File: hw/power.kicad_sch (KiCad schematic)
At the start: 0 parts

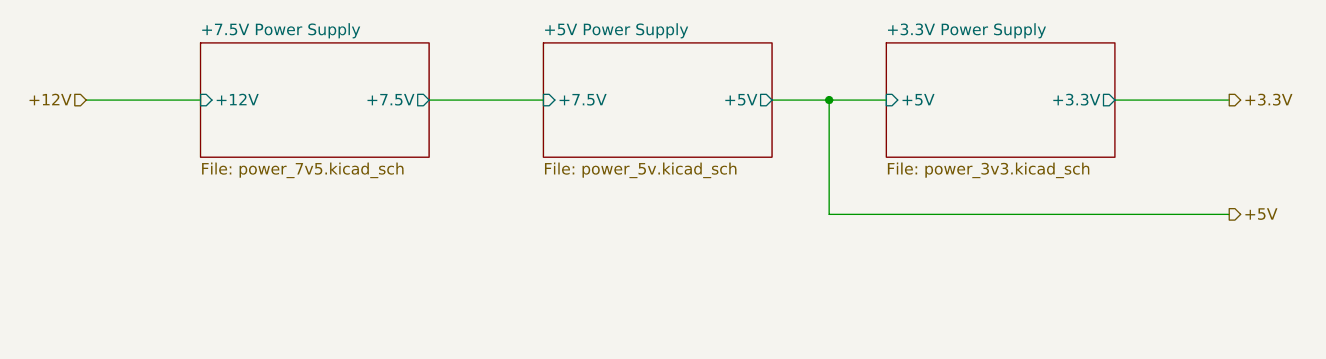
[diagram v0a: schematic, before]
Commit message: hw: top level schematic
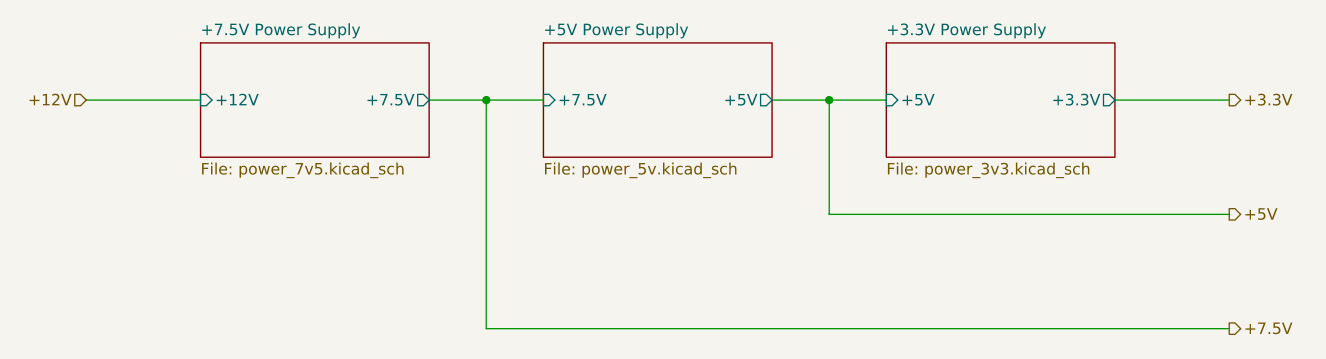
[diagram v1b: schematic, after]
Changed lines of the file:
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@@
+		(color 0 0 0 0)
+	)
+	(junction
+		(at 69.85 57.15)
+		(diameter 0)
 		(color 0 0 0 0)
 	)
 	(wire
 		(pts
-			(xy 63.5 57.15) (xy 76.2 57.15)
+			(xy 63.5 57.15) (xy 69.85 57.15)
 		)
 		(stroke
@@
 		)
 	)
+	(wire
+		(pts
+			(xy 69.85 82.55) (xy 152.4 82.55)
+		)
+		(stroke
+			(width 0)
+			(type default)
+		)
+	)
+	(wire
+		(pts
+			(xy 69.85 57.15) (xy 69.85 82.55)
+		)
+		(stroke
+			(width 0)
+			(type default)
+		)
+	)
+	(wire
+		(pts
+			(xy 69.85 57.15) (xy 76.2 57.15)
+		)
+		(stroke
+			(width 0)
+			(type default)
+		)
+	)
 	(hierarchical_label "+12V"
 		(shape input)
@@
 		(effects
 			(font
+				(size 1.27 1.27)
+			)
+			(justify left)
+		)
+	)
+	(hierarchical_label "+7.5V"
+		(shape output)
+		(at 152.4 82.55 0)
+		(effects
+			(font
